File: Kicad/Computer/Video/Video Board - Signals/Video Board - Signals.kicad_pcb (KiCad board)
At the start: 2 copper layers, 248.9 x 161.9 mm, 41 parts, among them IC1 LD1117S50C, IC2 SST39VF010-70-4I-NHE, IC3 74LVC573APW,118, J1 Conn_01x08_Pin, J2 Conn_01x40_Pin, J3 Conn_01x40_Pin, J4 Conn_01x40_Pin, J5 395-098-520-350, J6 Conn_01x08_Pin

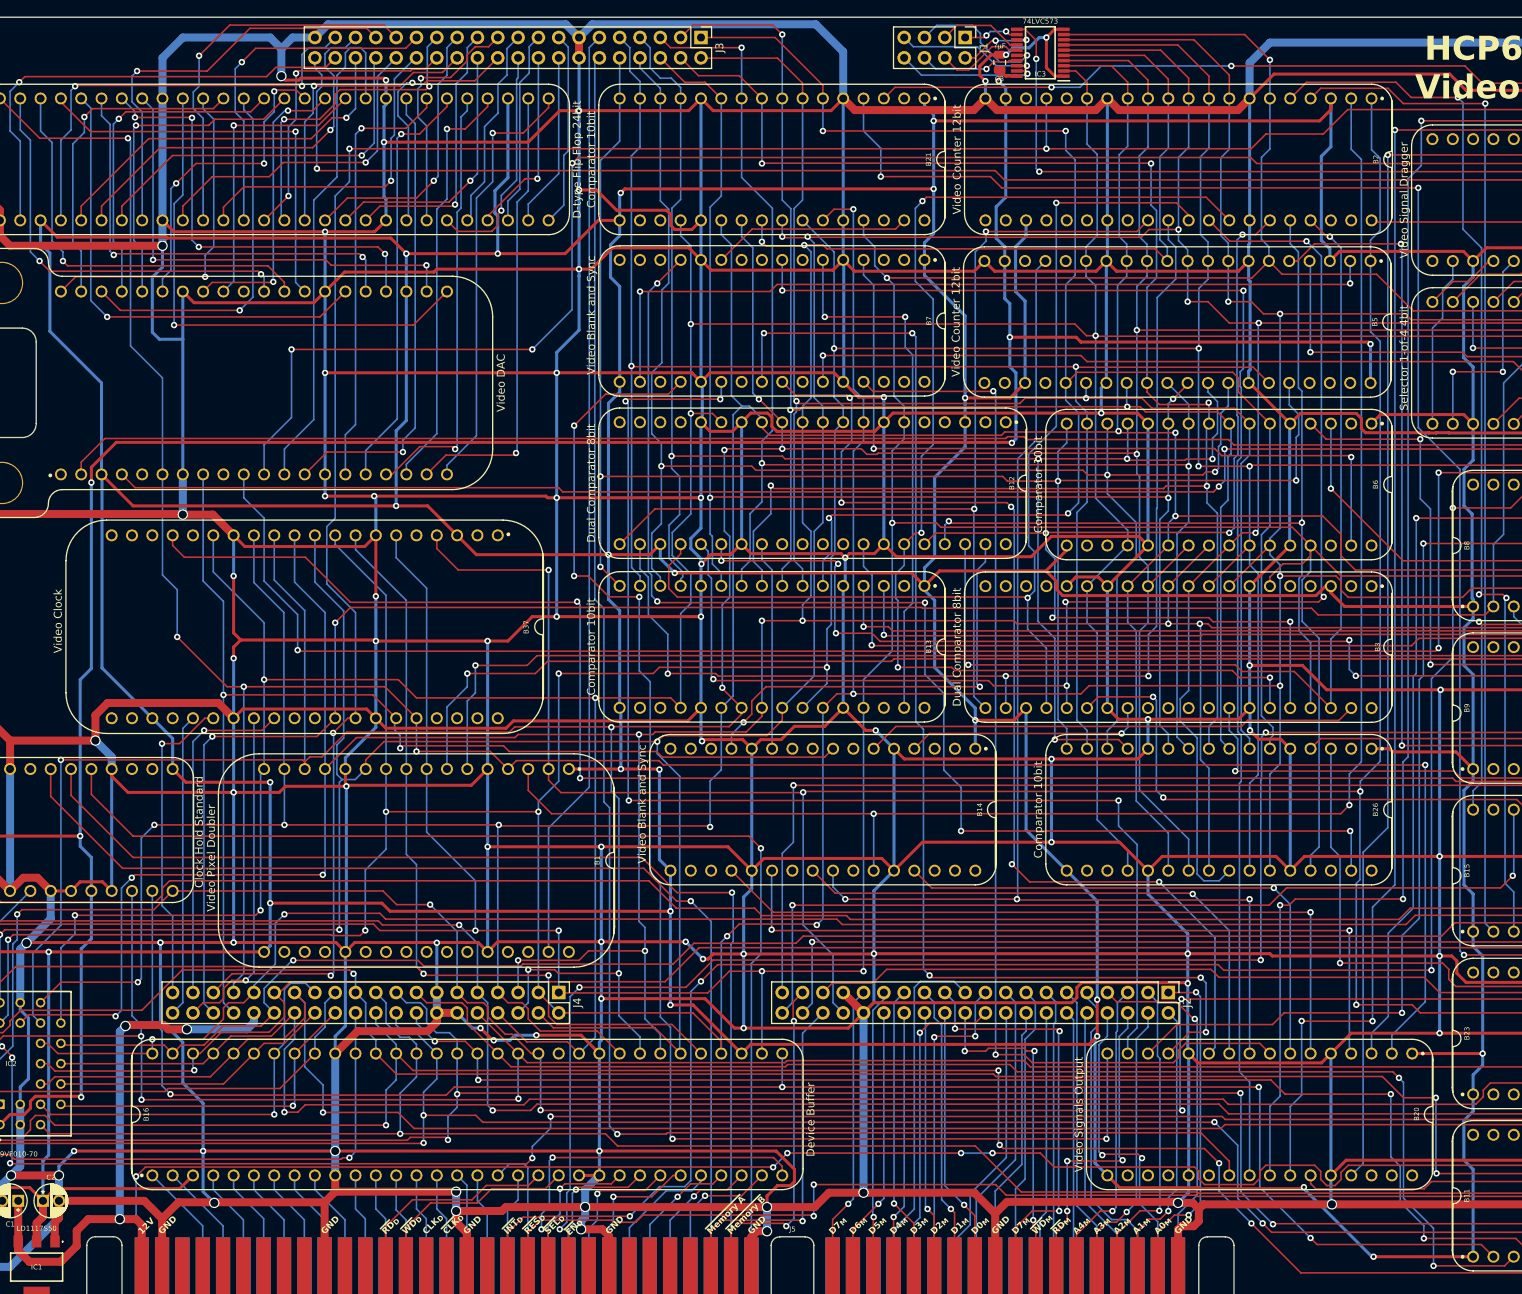
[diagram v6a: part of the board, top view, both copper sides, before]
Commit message: Added Video board renders.
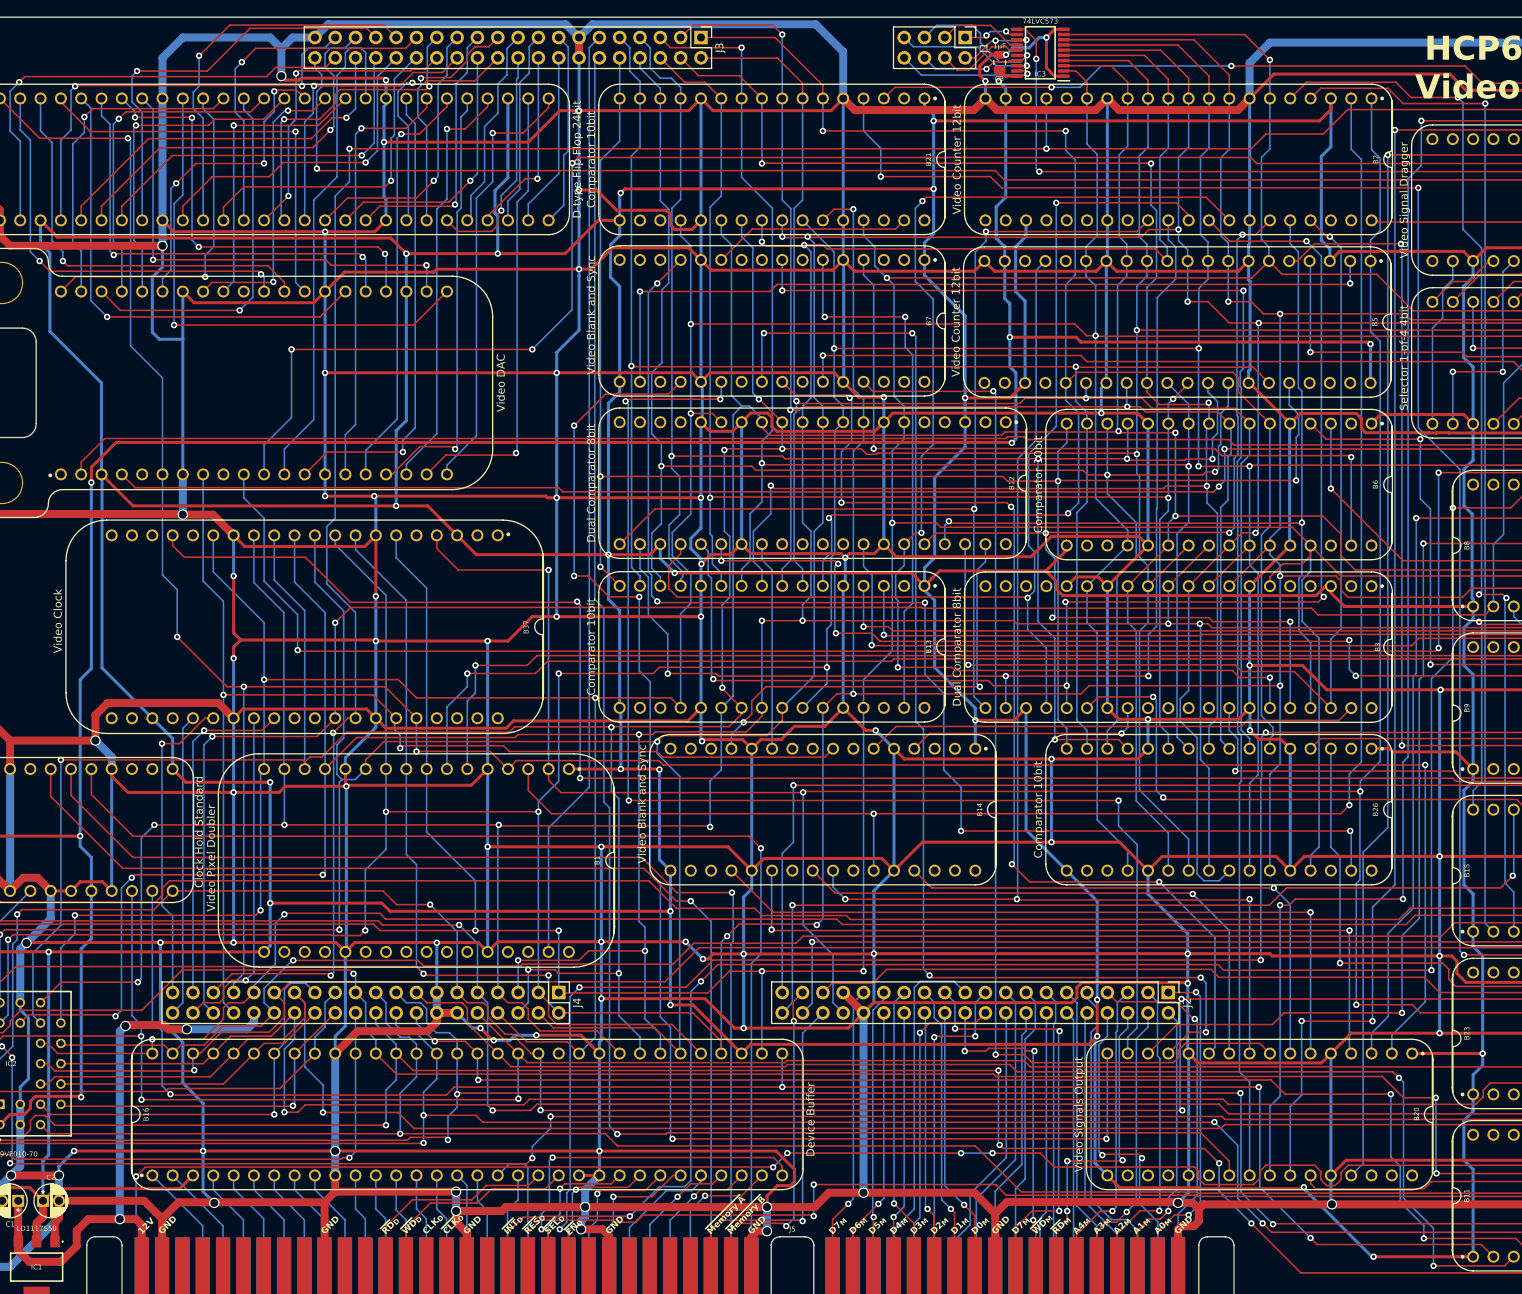
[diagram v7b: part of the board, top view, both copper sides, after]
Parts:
- C3: value ?μF -> 1μF
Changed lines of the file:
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@@
 	(paper "A4")
 	(title_block
-		(title "HCP65 Video Board")
+		(title "HCP65 Video Board Signals")
 		(date "2024-08-26")
 		(rev "V0")
@@
 		(model "${KICAD6_3DMODEL_DIR}/LED_THT.3dshapes/LED_D5.0mm.wrl"
 			(offset
-				(xyz 0 0 0)
+				(xyz 0 0 -2.8)
 			)
 			(scale
@@
 		(fp_arc
 			(start 86.040048 -8.4)
-			(mid 86.35762 -9.156489)
+			(mid 86.357626 -9.156454)
 			(end 87.117096 -9.466799)
 			(stroke
@@
 		(fp_arc
 			(start 90.297 -9.466799)
-			(mid 91.056441 -9.156453)
+			(mid 91.056476 -9.156459)
 			(end 91.374048 -8.4)
 			(stroke
@@
 		(fp_arc
 			(start 139.499048 -8.4)
-			(mid 139.81662 -9.156489)
+			(mid 139.816626 -9.156454)
 			(end 140.576096 -9.466799)
 			(stroke
@@
 		(fp_arc
 			(start 14.404267 -2.613733)
-			(mid 16.252453 -1.848189)
+			(mid 16.252451 -1.848184)
 			(end 17.017999 -0.000001)
 			(stroke
@@
 		(fp_arc
 			(start 14.404267 -2.613733)
-			(mid 16.252453 -1.848189)
+			(mid 16.252451 -1.848184)
 			(end 17.017999 -0.000001)
 			(stroke
@@
 		(fp_arc
 			(start 14.404267 -2.613733)
-			(mid 16.25245 -1.848186)
+			(mid 16.252448 -1.848183)
 			(end 17.017999 -0.000001)
 			(stroke
@@
 		(fp_arc
 			(start 14.404267 -2.613733)
-			(mid 16.252453 -1.848189)
+			(mid 16.252451 -1.848184)
 			(end 17.017999 -0.000001)
 			(stroke
@@
 		(fp_arc
 			(start 24.763183 0.179239)
-			(mid 25.272991 -1.051554)
+			(mid 25.272993 -1.051573)
 			(end 26.503802 -1.56138)
 			(stroke
@@
 		(fp_arc
 			(start 18.288 -4.826)
-			(mid 17.778172 -3.595211)
+			(mid 17.77817 -3.595211)
 			(end 16.547381 -3.085381)
 			(stroke
@@
 		(fp_arc
 			(start 14.404267 -2.613733)
-			(mid 16.252453 -1.848189)
+			(mid 16.252451 -1.848184)
 			(end 17.017999 -0.000001)
 			(stroke
@@
 			)
 		)
+		(property "Garbage" "Video Signals Output"
+			(at 0 0 -90)
+			(unlocked yes)
+			(layer "F.Fab")
+			(hide yes)
+			(effects
+				(font
+					(size 1 1)
+					(thickness 0.15)
+				)
+			)
+		)
 		(sheetname "Root")
 		(sheetfile "Video Board - Signals.kicad_sch")
@@
 		(fp_arc
 			(start 0.835733 40.713733)
-			(mid -1.012457 39.948189)
+			(mid -1.012457 39.94819)
 			(end -1.778 38.1)
 			(stroke
@@
 		(fp_arc
 			(start 14.404267 -2.613733)
-			(mid 16.252457 -1.84819)
+			(mid 16.252448 -1.848183)
 			(end 17.017999 -0.000001)
 			(stroke
@@
 		(fp_arc
 			(start 14.404267 -2.613733)
-			(mid 16.252453 -1.848189)
+			(mid 16.252451 -1.848184)
 			(end 17.017999 -0.000001)
 			(stroke
@@
 		(fp_arc
 			(start 14.404267 -2.613733)
-			(mid 16.252453 -1.848189)
+			(mid 16.252451 -1.848184)
 			(end 17.017999 -0.000001)
 			(stroke
@@
 			)
 		)
-		(property "Value" "?μF"
+		(property "Value" "1μF"
 			(at 0 2.032 180)
 			(layer "F.SilkS")
@@
 		(fp_arc
 			(start 0.835733 50.873733)
-			(mid -1.012457 50.108189)
+			(mid -1.012457 50.10819)
 			(end -1.778 48.26)
 			(stroke

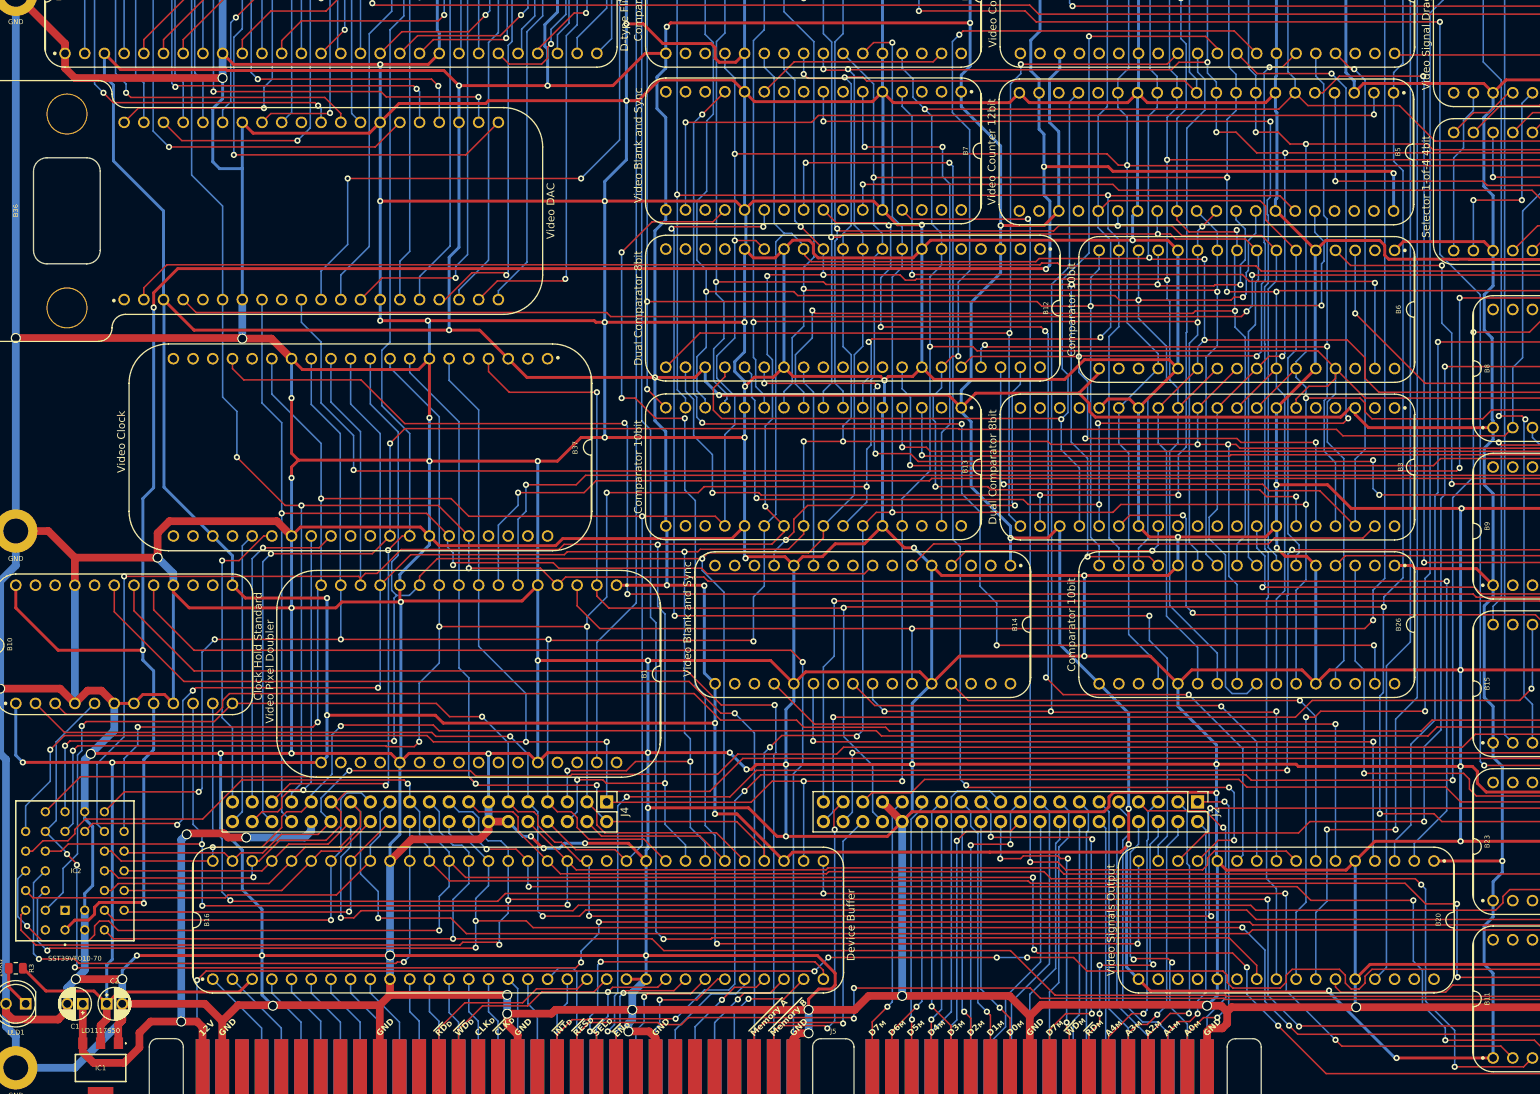
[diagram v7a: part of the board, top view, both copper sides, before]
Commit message: Reversed Video Board - Memory silkscreen.
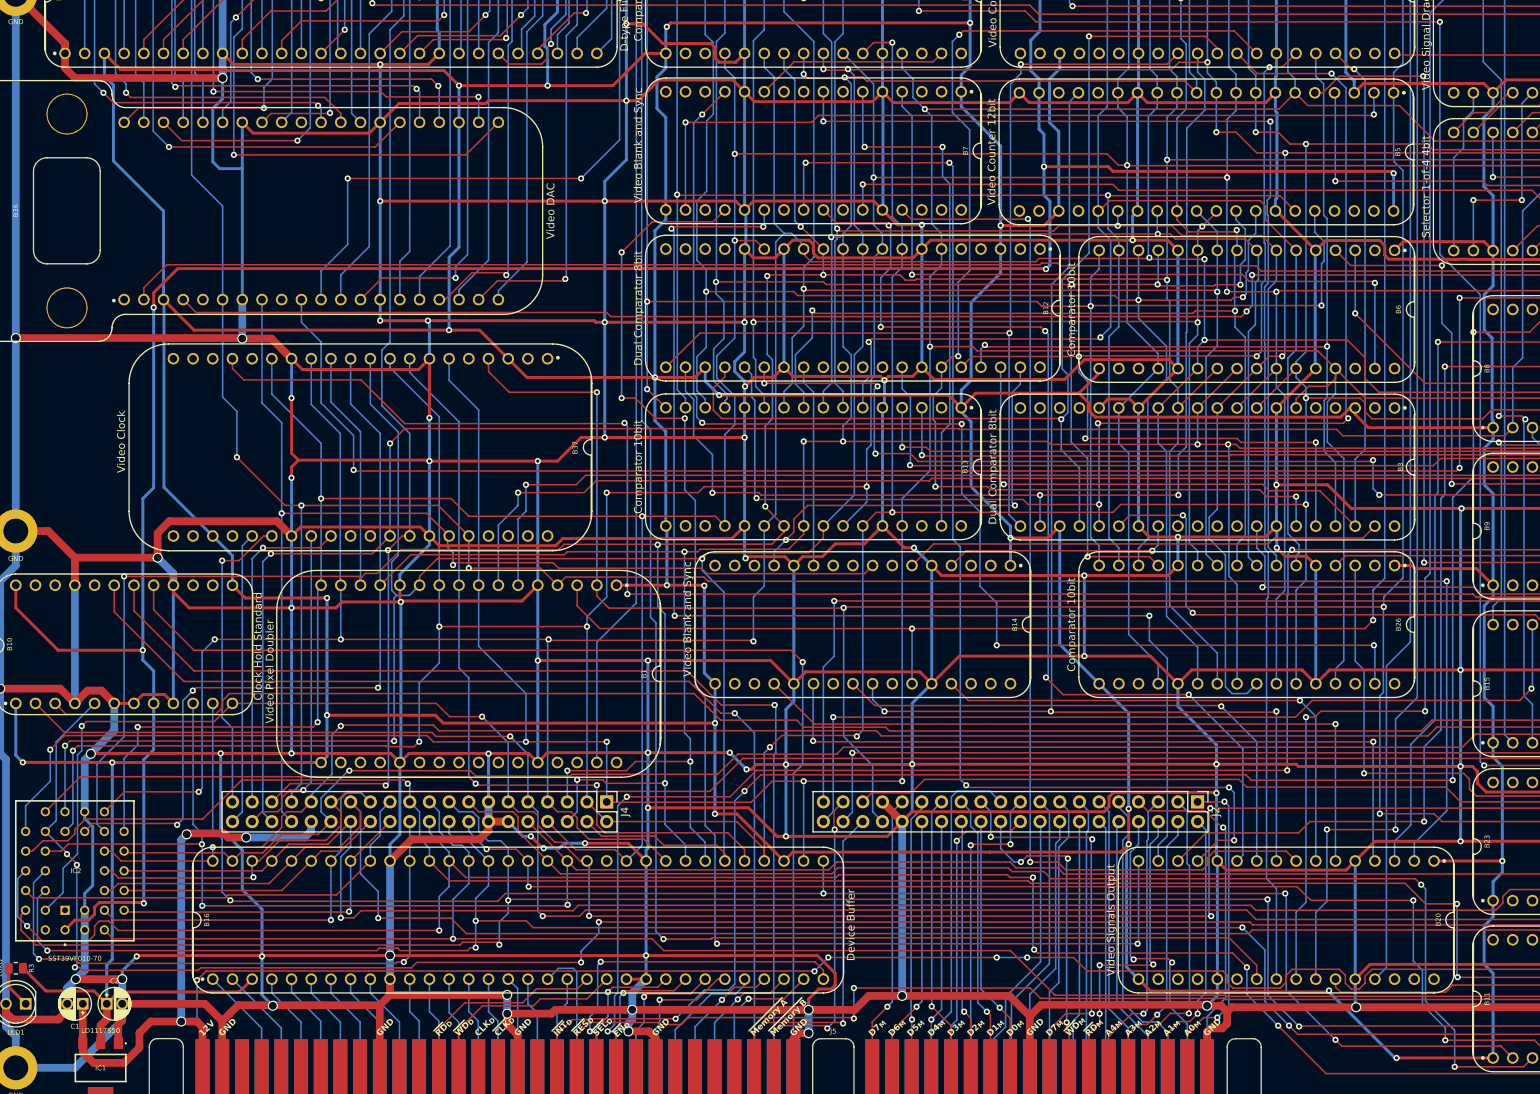
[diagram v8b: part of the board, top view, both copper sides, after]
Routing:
- net /D5: track 558.7 -> 559.5 mm
- net /~{RD}: track 307.1 -> 307.7 mm
- net /D4: track 559.5 -> 560.0 mm
